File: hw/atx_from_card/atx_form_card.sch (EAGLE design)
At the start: 26 parts

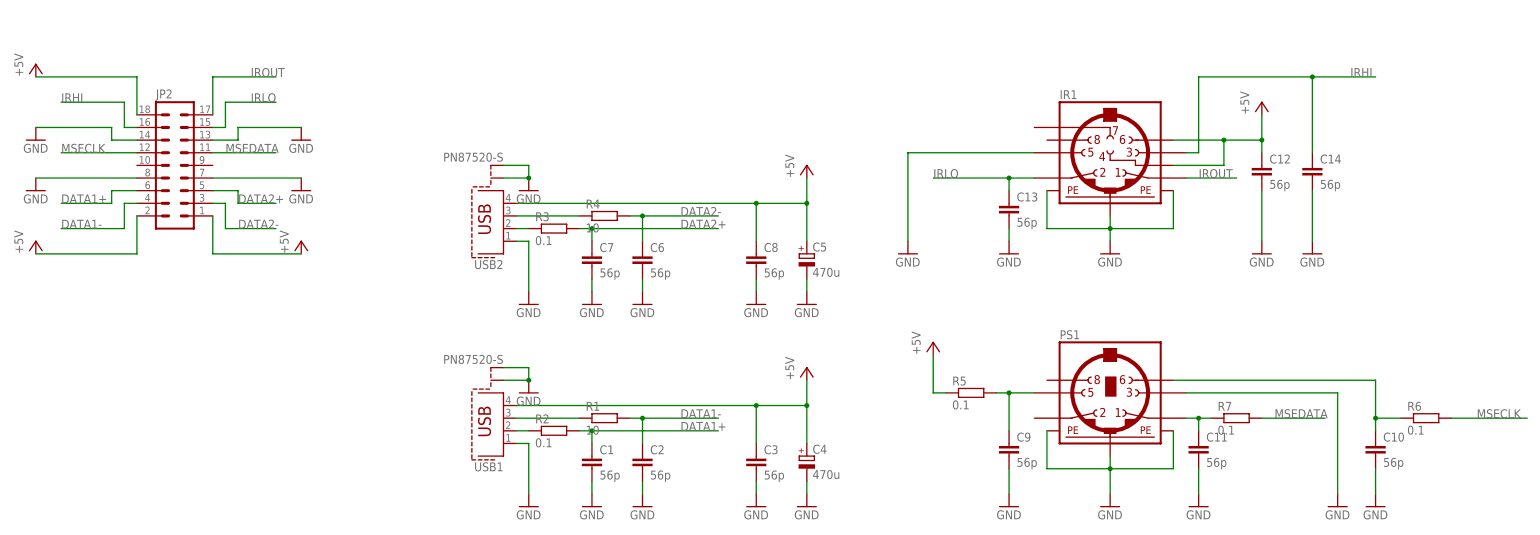
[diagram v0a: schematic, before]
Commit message: Changed lstb library to match pin numeration convention to original. Added additional 4x2 pin USB connector. Changed component numeration to match original. Routed the board. Fixed .gitignore for board and library old versions.
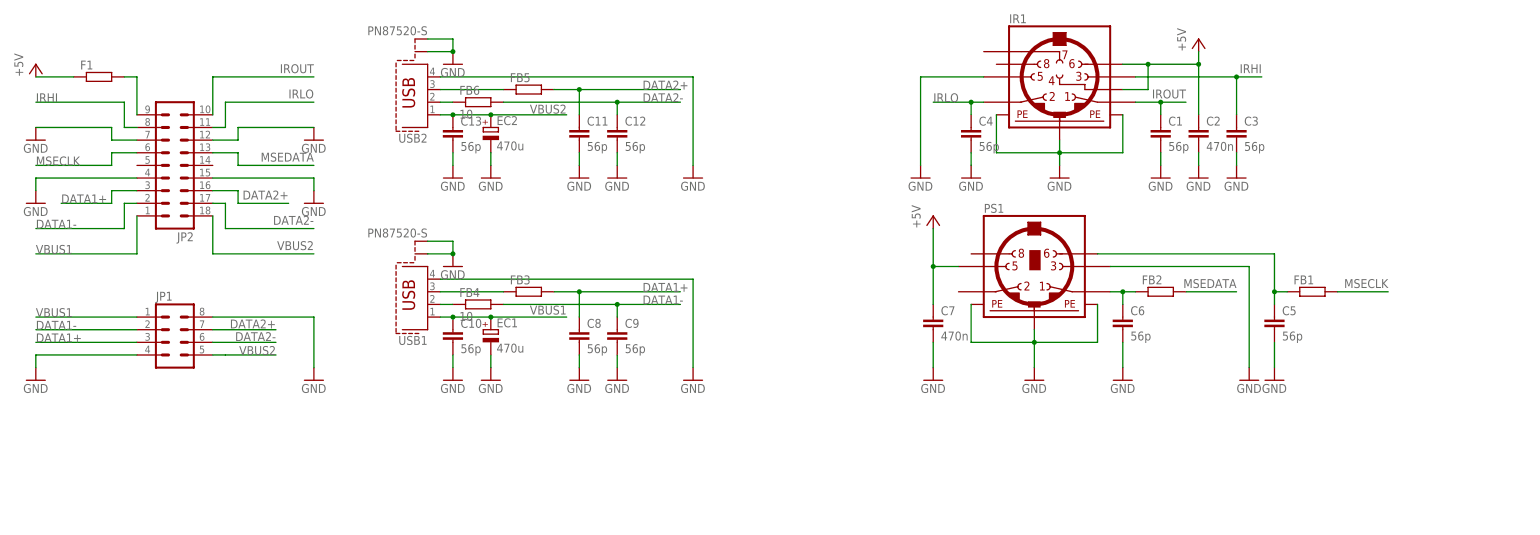
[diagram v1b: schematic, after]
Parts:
- removed C14: 56p, resistor:C-EUC3216
- removed R1, R4: 10, resistor:R-EU_M3216
- removed R2, R3, R5, R6, R7: 0.1, resistor:R-EU_M3216
- added EC1, EC2: 470u, resistor:CPOL-EUE2.5-6
- added F1: (no value), resistor:R-EU_0207/10
- added FB1, FB2, FB3, FB5: (no value), resistor:R-EU_M3216
- added FB4, FB6: 10, resistor:R-EU_M3216
- added JP1: (no value), con-lstb-custom:MA04-2
- C2, C7: value 56p -> 470n
- C4, C5: value 470u -> 56p; device resistor:CPOL-EUE2.5-6 -> resistor:C-EUC3216
- JP2: device con-lstb:MA09-2 -> con-lstb-custom:MA09-2
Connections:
- removed net N$7: C9.1, PS1.5, R5.2
- new net N$8: F1.2, JP2.9_
- new net VBUS1: C10.1, EC1.+, JP1.1, JP2.1_, USB1.1
- new net VBUS2: C13.1, EC2.+, JP1.5, JP2.10_, USB2.1
- net DATA1+: now also C8.1, FB3.2, JP1.3, JP2.3_; no longer C1.1, JP2.6, R2.2
- net DATA1-: now also C9.1, FB4.2, JP1.2, JP2.2_; no longer C2.1, JP2.4, R1.2
- net DATA2+: now also C11.1, FB5.2, JP1.7, JP2.12_; no longer C7.1, JP2.5, R3.2
- net DATA2-: now also C12.1, FB6.2, JP1.6, JP2.11_; no longer C6.1, JP2.3, R4.2
- net GND: now also C4.2, C5.2, EC1.-, EC2.-, JP1.4, JP1.8, JP2.13_, JP2.16_, JP2.4_, JP2.7_, USB1.4, USB2.4; no longer C14.2, C4.-, C5.-, JP2.13, JP2.14, JP2.7, JP2.8, USB1.1, USB2.1
- net IRHI: now also C3.1, JP2.8_; no longer C14.1, JP2.16
- net IRLO: now also C4.1, JP2.17_; no longer C13.1, JP2.15
- net IROUT: now also C1.1, JP2.18_; no longer JP2.17
- net MSECLK: now also FB1.2, JP2.6_; no longer JP2.12, R6.2
- net MSEDATA: now also FB2.2, JP2.15_; no longer JP2.11, R7.2
- net N$1: now also FB4.1; no longer R2.1
- net N$2: now also C6.1, FB2.1; no longer C11.1, R7.1
- net N$3: now also FB6.1; no longer R3.1
- net N$4: now also FB3.1; no longer R1.1
- net N$5: now also FB5.1; no longer R4.1
- net N$6: now also C5.1, FB1.1; no longer C10.1, R6.1
- net VCC: now also C2.1, C7.1, F1.1, PS1.5; no longer C12.1, C3.1, C4.+, C5.+, C8.1, JP2.1, JP2.18, JP2.2, R5.1, USB1.4, USB2.4
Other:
- moved on the sheet: C1, C10, C11, C12, C13, C2, C3, C6, C7, C8, C9, IR1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

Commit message: Rev. D of the board. Added more documentation.
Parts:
- C1, C10, C11, C12, C13, C2, C3, C4, C5, C6, C7, C8, C9: device resistor:C-EUC3216 -> resistor-custom:C-EUC3216
- EC1, EC2: device resistor:CPOL-EUE2.5-6 -> resistor-custom:CPOL-EUE3.5-8
- F1: device resistor:R-EU_0207/10 -> resistor-custom:R-EU_0207/10
- FB1, FB2, FB3, FB4, FB5, FB6: device resistor:R-EU_M3216 -> resistor-custom:R-EU_M3216
- USB1, USB2: device con-berg:PN87520-S -> con-berg-custom:PN87520-S
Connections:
- net VCC: no longer IR1.6
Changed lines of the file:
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@@
 </classes>
 <parts>
-<part name="USB1" library="con-berg" deviceset="PN87520-S" device=""/>
+<part name="USB1" library="con-berg-custom" deviceset="PN87520-S" device=""/>
 <part name="JP2" library="con-lstb-custom" deviceset="MA09-2" device=""/>
 <part name="PS1" library="mini_din" deviceset="MINI_DIN_6" device=""/>
@@
 <part name="GND3" library="supply1" deviceset="GND" device=""/>
 <part name="GND4" library="supply1" deviceset="GND" device=""/>
-<part name="FB3" library="resistor" deviceset="R-EU_" device="M3216"/>
+<part name="FB3" library="resistor-custom" deviceset="R-EU_" device="M3216"/>
 <part name="GND5" library="supply1" deviceset="GND" device=""/>
-<part name="C8" library="resistor" deviceset="C-EU" device="C3216" value="56p"/>
+<part name="C8" library="resistor-custom" deviceset="C-EU" device="C3216" value="56p"/>
 <part name="GND6" library="supply1" deviceset="GND" device=""/>
-<part name="FB4" library="resistor" deviceset="R-EU_" device="M3216" value="10"/>
-<part name="C9" library="resistor" deviceset="C-EU" device="C3216" value="56p"/>
+<part name="FB4" library="resistor-custom" deviceset="R-EU_" device="M3216" value="10"/>
+<part name="C9" library="resistor-custom" deviceset="C-EU" device="C3216" value="56p"/>
 <part name="GND7" library="supply1" deviceset="GND" device=""/>
 <part name="GND8" library="supply1" deviceset="GND" device=""/>
-<part name="C10" library="resistor" deviceset="C-EU" device="C3216" value="56p"/>
-<part name="EC1" library="resistor" deviceset="CPOL-EU" device="E2.5-6" value="470u"/>
+<part name="C10" library="resistor-custom" deviceset="C-EU" device="C3216" value="56p"/>
+<part name="EC1" library="resistor-custom" deviceset="CPOL-EU" device="E3.5-8" value="470u"/>
 <part name="GND9" library="supply1" deviceset="GND" device=""/>
 <part name="GND10" library="supply1" deviceset="GND" device=""/>
-<part name="USB2" library="con-berg" deviceset="PN87520-S" device=""/>
-<part name="FB5" library="resistor" deviceset="R-EU_" device="M3216"/>
+<part name="USB2" library="con-berg-custom" deviceset="PN87520-S" device=""/>
+<part name="FB5" library="resistor-custom" deviceset="R-EU_" device="M3216"/>
 <part name="GND11" library="supply1" deviceset="GND" device=""/>
-<part name="C11" library="resistor" deviceset="C-EU" device="C3216" value="56p"/>
+<part name="C11" library="resistor-custom" deviceset="C-EU" device="C3216" value="56p"/>
 <part name="GND12" library="supply1" deviceset="GND" device=""/>
-<part name="FB6" library="resistor" deviceset="R-EU_" device="M3216" value="10"/>
-<part name="C12" library="resistor" deviceset="C-EU" device="C3216" value="56p"/>
+<part name="FB6" library="resistor-custom" deviceset="R-EU_" device="M3216" value="10"/>
+<part name="C12" library="resistor-custom" deviceset="C-EU" device="C3216" value="56p"/>
 <part name="GND13" library="supply1" deviceset="GND" device=""/>
 <part name="GND14" library="supply1" deviceset="GND" device=""/>
-<part name="C13" library="resistor" deviceset="C-EU" device="C3216" value="56p"/>
-<part name="EC2" library="resistor" deviceset="CPOL-EU" device="E2.5-6" value="470u"/>
+<part name="C13" library="resistor-custom" deviceset="C-EU" device="C3216" value="56p"/>
+<part name="EC2" library="resistor-custom" deviceset="CPOL-EU" device="E3.5-8" value="470u"/>
 <part name="GND15" library="supply1" deviceset="GND" device=""/>
 <part name="GND16" library="supply1" deviceset="GND" device=""/>
 <part name="GND17" library="supply1" deviceset="GND" device=""/>
-<part name="C6" library="resistor" deviceset="C-EU" device="C3216" value="56p"/>
+<part name="C6" library="resistor-custom" deviceset="C-EU" device="C3216" value="56p"/>
 <part name="GND18" library="supply1" deviceset="GND" device=""/>
 <part name="GND19" library="supply1" deviceset="GND" device=""/>
-<part name="FB2" library="resistor" deviceset="R-EU_" device="M3216"/>
-<part name="C5" library="resistor" deviceset="C-EU" device="C3216" value="56p"/>
-<part name="FB1" library="resistor" deviceset="R-EU_" device="M3216"/>
+<part name="FB2" library="resistor-custom" deviceset="R-EU_" device="M3216"/>
+<part name="C5" library="resistor-custom" deviceset="C-EU" device="C3216" value="56p"/>
+<part name="FB1" library="resistor-custom" deviceset="R-EU_" device="M3216"/>
 <part name="GND20" library="supply1" deviceset="GND" device=""/>
-<part name="C7" library="resistor" deviceset="C-EU" device="C3216" value="470n"/>
-<part name="F1" library="resistor" deviceset="R-EU_" device="0207/10"/>
+<part name="C7" library="resistor-custom" deviceset="C-EU" device="C3216" value="470n"/>
+<part name="F1" library="resistor-custom" deviceset="R-EU_" device="0207/10"/>
 <part name="P+7" library="supply1" deviceset="VCC" device="" value="+5V"/>
 <part name="GND21" library="supply1" deviceset="GND" device=""/>
-<part name="C2" library="resistor" deviceset="C-EU" device="C3216" value="470n"/>
+<part name="C2" library="resistor-custom" deviceset="C-EU" device="C3216" value="470n"/>
 <part name="P+8" library="supply1" deviceset="VCC" device="" value="+5V"/>
 <part name="GND22" library="supply1" deviceset="GND" device=""/>
 <part name="GND23" library="supply1" deviceset="GND" device=""/>
-<part name="C4" library="resistor" deviceset="C-EU" device="C3216" value="56p"/>
+<part name="C4" library="resistor-custom" deviceset="C-EU" device="C3216" value="56p"/>
 <part name="GND24" library="supply1" deviceset="GND" device=""/>
 <part name="GND25" library="supply1" deviceset="GND" device=""/>
-<part name="C3" library="resistor" deviceset="C-EU" device="C3216" value="56p"/>
+<part name="C3" library="resistor-custom" deviceset="C-EU" device="C3216" value="56p"/>
 <part name="GND26" library="supply1" deviceset="GND" device=""/>
 <part name="JP1" library="con-lstb-custom" deviceset="MA04-2" device=""/>
 <part name="GND27" library="supply1" deviceset="GND" device=""/>
 <part name="GND28" library="supply1" deviceset="GND" device=""/>
-<part name="C1" library="resistor" deviceset="C-EU" device="C3216" value="56p"/>
+<part name="C1" library="resistor-custom" deviceset="C-EU" device="C3216" value="56p"/>
 <part name="GND29" library="supply1" deviceset="GND" device=""/>
 </parts>
@@
 </segment>
 <segment>
-<pinref part="IR1" gate="G$1" pin="6"/>
-<wire x1="226.06" y1="68.58" x2="231.14" y2="68.58" width="0.1524" layer="91"/>
 <wire x1="231.14" y1="68.58" x2="231.14" y2="63.5" width="0.1524" layer="91"/>
 <pinref part="IR1" gate="G$1" pin="4"/>
@@
 <pinref part="C2" gate="G$1" pin="1"/>
 <wire x1="241.3" y1="68.58" x2="241.3" y2="58.42" width="0.1524" layer="91"/>
-<junction x="231.14" y="68.58"/>
 <junction x="241.3" y="68.58"/>
 </segment>
